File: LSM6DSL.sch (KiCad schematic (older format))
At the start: 6 parts, among them J1 Conn_01x10, U1 LSM6DSL

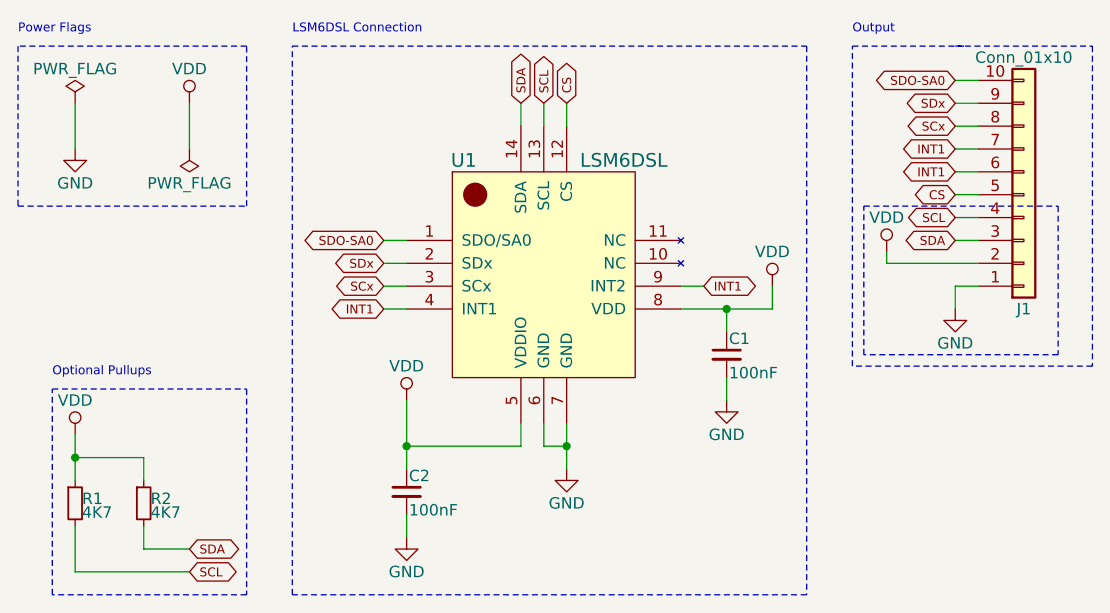
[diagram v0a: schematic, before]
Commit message: Fixed wrong label INT1
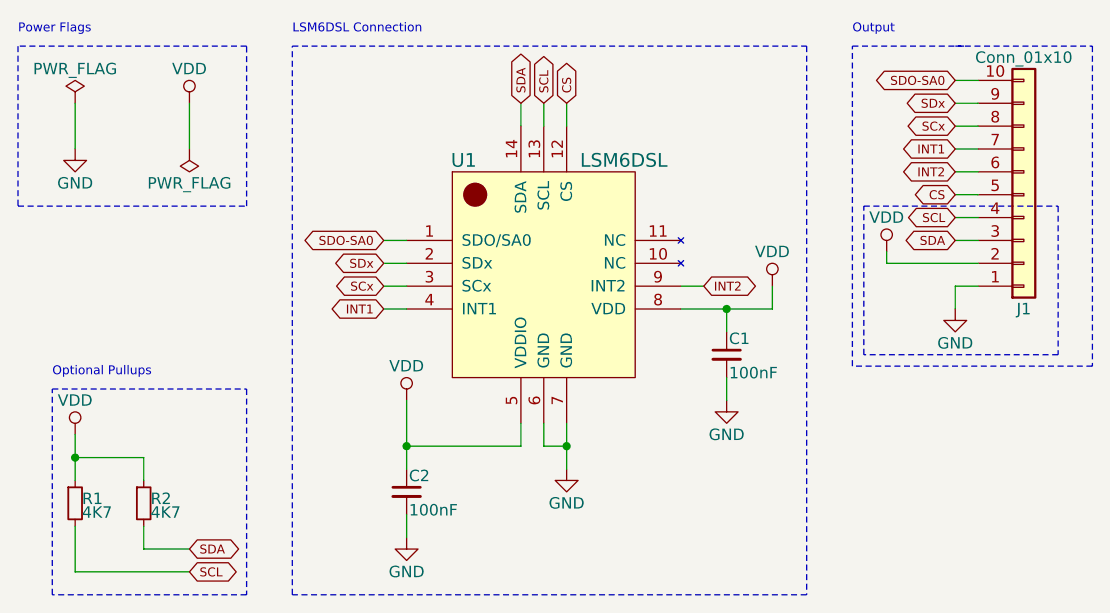
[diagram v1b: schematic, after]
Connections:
- net INT1: no longer J1.6 (Pin_6), U1.9 (INT2)
- new net INT2: J1.6 (Pin_6), U1.9 (INT2)
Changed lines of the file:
@@
 LIBS:valves
 LIBS:lsm6dsl-breakout
+LIBS:LSM6DSL-cache
 EELAYER 25 0
 EELAYER END
@@
 $EndDescr
 $Comp
-L GND #PWR9
+L GND #PWR01
 U 1 1 5AA19CD9
 P 5850 4450
-F 0 "#PWR9" H 5850 4200 50  0001 C CNN
+F 0 "#PWR01" H 5850 4200 50  0001 C CNN
 F 1 "GND" H 5850 4300 50  0000 C CNN
 F 2 "" H 5850 4450 50  0001 C CNN
@@
 $EndComp
 $Comp
-L GND #PWR7
+L GND #PWR02
 U 1 1 5AA19F30
 P 6550 4150
-F 0 "#PWR7" H 6550 3900 50  0001 C CNN
+F 0 "#PWR02" H 6550 3900 50  0001 C CNN
 F 1 "GND" H 6550 4000 50  0000 C CNN
 F 2 "" H 6550 4150 50  0001 C CNN
@@
 $EndComp
 $Comp
-L VDD #PWR4
+L VDD #PWR03
 U 1 1 5AA19FE4
 P 6750 3650
-F 0 "#PWR4" H 6750 3500 50  0001 C CNN
+F 0 "#PWR03" H 6750 3500 50  0001 C CNN
 F 1 "VDD" H 6750 3800 50  0000 C CNN
 F 2 "" H 6750 3650 50  0001 C CNN
@@
 $EndComp
 $Comp
-L GND #PWR10
+L GND #PWR04
 U 1 1 5AA1A229
 P 5150 4750
-F 0 "#PWR10" H 5150 4500 50  0001 C CNN
+F 0 "#PWR04" H 5150 4500 50  0001 C CNN
 F 1 "GND" H 5150 4600 50  0000 C CNN
 F 2 "" H 5150 4750 50  0001 C CNN
@@
 CS
 Text GLabel 6450 3650 2    39   BiDi ~ 0
-INT1
+INT2
 Text GLabel 5750 2850 1    39   BiDi ~ 0
 SCL
@@
 LSM6DSL Connection
 $Comp
-L VDD #PWR6
+L VDD #PWR05
 U 1 1 5AA1AB15
 P 5150 4150
-F 0 "#PWR6" H 5150 4000 50  0001 C CNN
+F 0 "#PWR05" H 5150 4000 50  0001 C CNN
 F 1 "VDD" H 5150 4300 50  0000 C CNN
 F 2 "" H 5150 4150 50  0001 C CNN
@@
 $EndComp
 $Comp
-L VDD #PWR8
+L VDD #PWR06
 U 1 1 5AA1AB2F
 P 3700 4300
-F 0 "#PWR8" H 3700 4150 50  0001 C CNN
+F 0 "#PWR06" H 3700 4150 50  0001 C CNN
 F 1 "VDD" H 3700 4450 50  0000 C CNN
 F 2 "" H 3700 4300 50  0001 C CNN
@@
 $EndComp
 $Comp
-L VDD #PWR1
+L VDD #PWR07
 U 1 1 5AA1AB5D
 P 4200 2850
-F 0 "#PWR1" H 4200 2700 50  0001 C CNN
+F 0 "#PWR07" H 4200 2700 50  0001 C CNN
 F 1 "VDD" H 4200 3000 50  0000 C CNN
 F 2 "" H 4200 2850 50  0001 C CNN
@@
 $EndComp
 $Comp
-L GND #PWR2
+L GND #PWR08
 U 1 1 5AA1AB77
 P 3700 3050
-F 0 "#PWR2" H 3700 2800 50  0001 C CNN
+F 0 "#PWR08" H 3700 2800 50  0001 C CNN
 F 1 "GND" H 3700 2900 50  0000 C CNN
 F 2 "" H 3700 3050 50  0001 C CNN
@@
 $EndComp
 $Comp
-L PWR_FLAG #FLG1
+L PWR_FLAG #FLG09
 U 1 1 5AA1AB8E
 P 3700 2850
-F 0 "#FLG1" H 3700 2925 50  0001 C CNN
+F 0 "#FLG09" H 3700 2925 50  0001 C CNN
 F 1 "PWR_FLAG" H 3700 3000 50  0000 C CNN
 F 2 "" H 3700 2850 50  0001 C CNN
@@
 $EndComp
 $Comp
-L PWR_FLAG #FLG2
+L PWR_FLAG #FLG010
 U 1 1 5AA1AC1D
 P 4200 3050
-F 0 "#FLG2" H 4200 3125 50  0001 C CNN
+F 0 "#FLG010" H 4200 3125 50  0001 C CNN
 F 1 "PWR_FLAG" H 4200 3200 50  0000 C CNN
 F 2 "" H 4200 3050 50  0001 C CNN
@@
 $EndComp
 $Comp
-L VDD #PWR3
+L VDD #PWR011
 U 1 1 5AA1AEFF
 P 7250 3500
-F 0 "#PWR3" H 7250 3350 50  0001 C CNN
+F 0 "#PWR011" H 7250 3350 50  0001 C CNN
 F 1 "VDD" H 7250 3650 50  0000 C CNN
 F 2 "" H 7250 3500 50  0001 C CNN
@@
 $EndComp
 $Comp
-L GND #PWR5
+L GND #PWR012
 U 1 1 5AA1AF1C
 P 7550 3750
-F 0 "#PWR5" H 7550 3500 50  0001 C CNN
+F 0 "#PWR012" H 7550 3500 50  0001 C CNN
 F 1 "GND" H 7550 3600 50  0000 C CNN
 F 2 "" H 7550 3750 50  0001 C CNN
@@
 CS
 Text GLabel 7550 3150 0    39   BiDi ~ 0
-INT1
+INT2
 Text GLabel 7550 3050 0    39   BiDi ~ 0
 INT1
